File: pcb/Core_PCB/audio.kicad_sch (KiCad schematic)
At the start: 3 parts, among them J1 Screw_Terminal_01x02, U1 MAX98357A

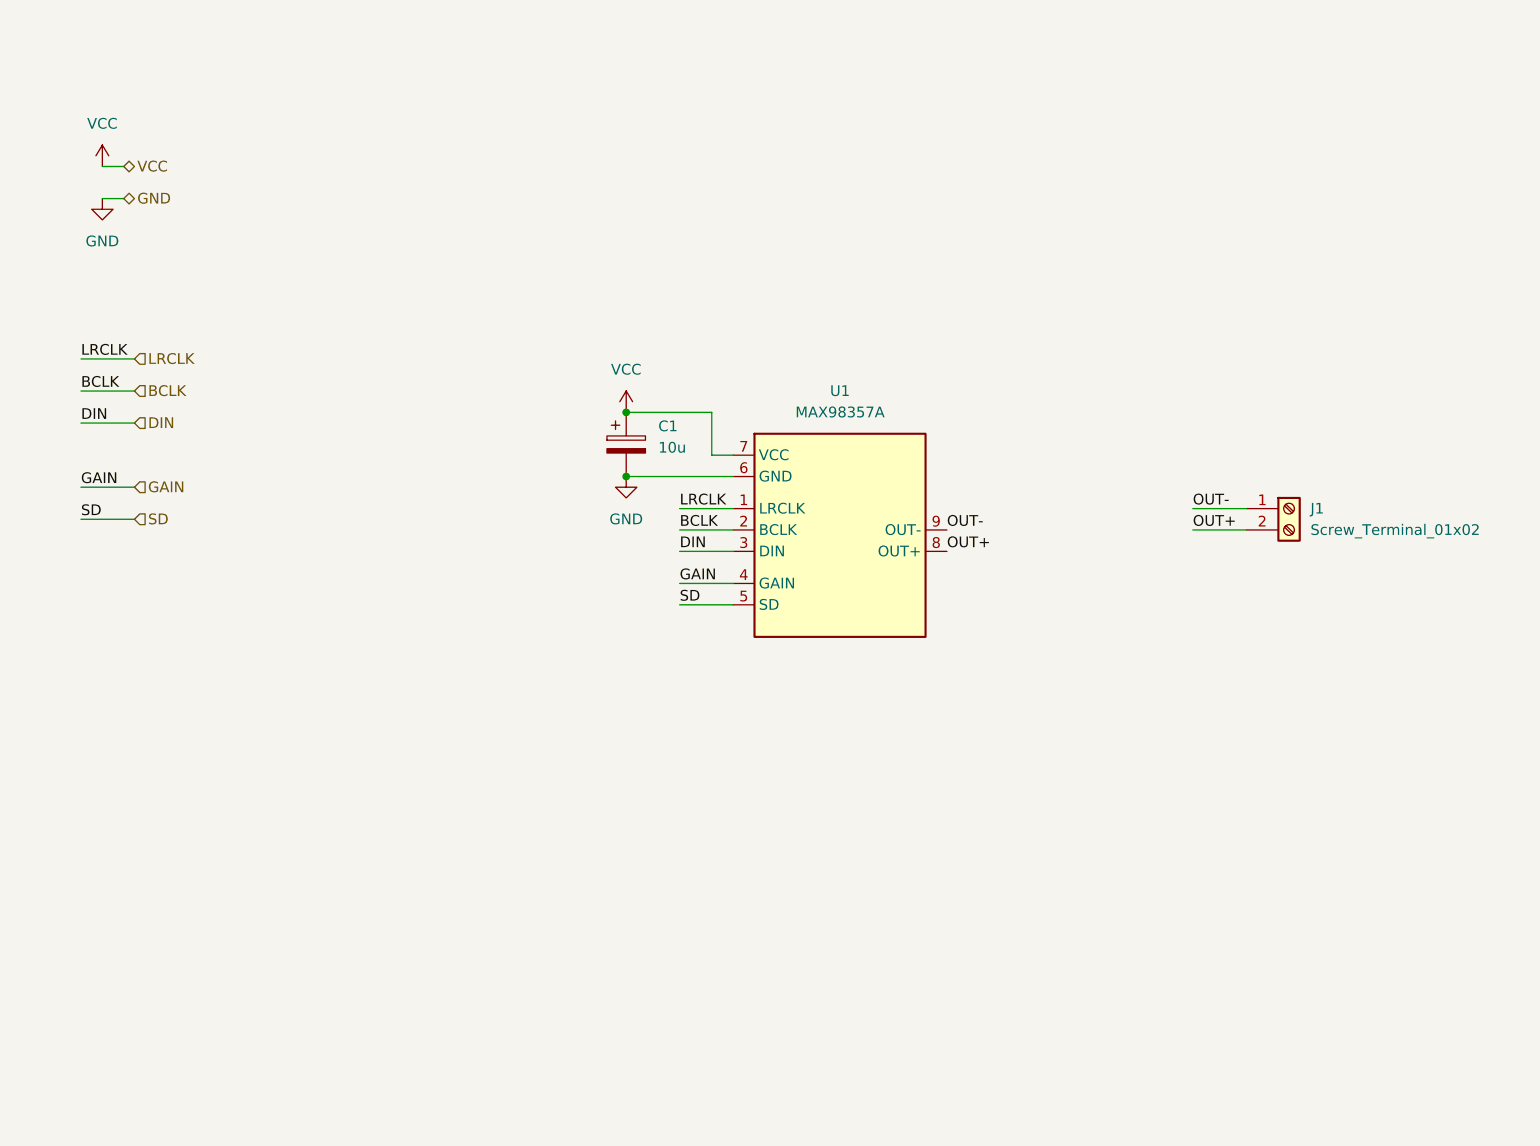
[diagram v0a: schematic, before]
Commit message: SCH: audio gain control via mux (HEF4051), buttons read via i2c io expander (MCP23017)
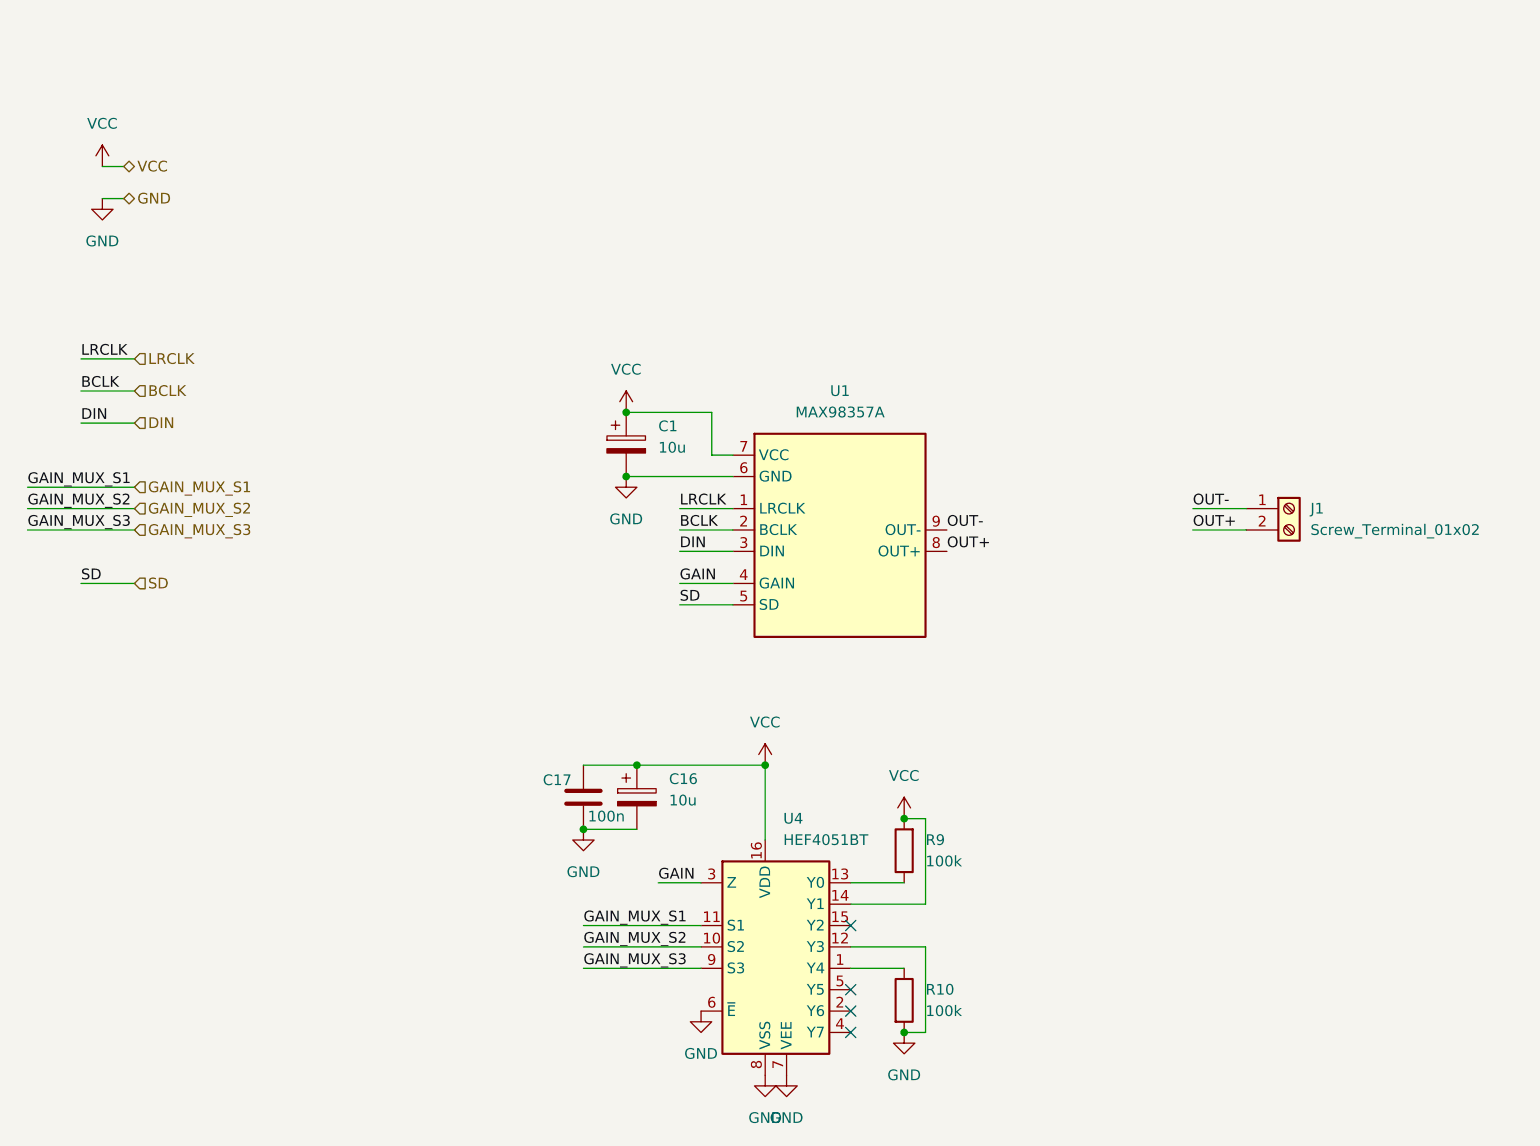
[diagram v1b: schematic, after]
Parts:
- added C16: 10u, symbol Device:C_Polarized
- added C17: 100n, symbol Device:C
- added R10, R9: 100k, symbol Device:R
- added U4: HEF4051BT, Package_SO:SOIC-16_3.9x9.9mm_P1.27mm, symbol Analog_Switch:HEF4051BT
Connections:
- net GAIN: now also U4.3 (Z)
- net GND: now also C16.2, C17.2, R10.2, U4.12 (Y3), U4.6 (~{E}), U4.7 (VEE), U4.8 (VSS)
- net VCC: now also C16.1, C17.1, R9.2, U4.14 (Y1), U4.16 (VDD)
- new net: R10.1, U4.1 (Y4)
- new net: R9.1, U4.13 (Y0)
- new net GAIN_MUX_S1: U4.11 (S1)
- new net GAIN_MUX_S2: U4.10 (S2)
- new net GAIN_MUX_S3: U4.9 (S3)
- no-connect marks 0 -> 4

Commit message: SCH: annotated sheets, reannotated all components
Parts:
- J6: renamed from J1; Name (none) -> SPEAKER
- renumbered C1 to C4, C17 to C5, C16 to C6, R9 to R1, R10 to R2, U4 to U2
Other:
- company: (none) -> brunolalb@gmail.com
- title: (none) -> Alarm Clock Resto Mod - Core PCB
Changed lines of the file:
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@@
 	(generator_version "10.0")
 	(paper "A4")
+	(title_block
+		(title "Alarm Clock Resto Mod - Core PCB")
+		(date "2026-07-08")
+		(rev "1.0")
+		(company "brunolalb@gmail.com")
+		(comment 1 "Bruno Landau Albrecht")
+	)
 	(junction
 		(at 102.87 76.2)
@@
 		(in_pos_files yes)
 		(dnp no)
-		(property "Reference" "C17"
+		(property "Reference" "C5"
 			(at 92.964 112.268 0)
 			(show_name no)
@@
 			(project "Core_PCB"
 				(path "/79975d02-cfea-4cc3-8869-9743c86248b2/277cf276-8816-41e6-a7a7-65f79c8908df"
-					(reference "C17")
+					(reference "C5")
 					(unit 1)
 				)
@@
 		(dnp no)
 		(fields_autoplaced yes)
-		(property "Reference" "#PWR014"
+		(property "Reference" "#PWR024"
 			(at 40.64 49.53 0)
 			(hide yes)
@@
 			(project "Core_PCB"
 				(path "/79975d02-cfea-4cc3-8869-9743c86248b2/277cf276-8816-41e6-a7a7-65f79c8908df"
-					(reference "#PWR014")
+					(reference "#PWR024")
 					(unit 1)
 				)
@@
 		(dnp no)
 		(fields_autoplaced yes)
-		(property "Reference" "#PWR052"
+		(property "Reference" "#PWR031"
 			(at 135.89 148.59 0)
 			(hide yes)
@@
 			(project "Core_PCB"
 				(path "/79975d02-cfea-4cc3-8869-9743c86248b2/277cf276-8816-41e6-a7a7-65f79c8908df"
-					(reference "#PWR052")
+					(reference "#PWR031")
 					(unit 1)
 				)
@@
 		(dnp no)
 		(fields_autoplaced yes)
-		(property "Reference" "#PWR055"
+		(property "Reference" "#PWR029"
 			(at 97.79 124.46 0)
 			(hide yes)
@@
 			(project "Core_PCB"
 				(path "/79975d02-cfea-4cc3-8869-9743c86248b2/277cf276-8816-41e6-a7a7-65f79c8908df"
-					(reference "#PWR055")
+					(reference "#PWR029")
 					(unit 1)
 				)
@@
 		(dnp no)
 		(fields_autoplaced yes)
-		(property "Reference" "U4"
+		(property "Reference" "U2"
 			(at 121.5233 116.84 0)
 			(show_name no)
@@
 			(project "Core_PCB"
 				(path "/79975d02-cfea-4cc3-8869-9743c86248b2/277cf276-8816-41e6-a7a7-65f79c8908df"
-					(reference "U4")
+					(reference "U2")
 					(unit 1)
 				)
@@
 		(dnp no)
 		(fields_autoplaced yes)
-		(property "Reference" "C16"
+		(property "Reference" "C6"
 			(at 107.95 112.1409 0)
 			(show_name no)
@@
 			(project "Core_PCB"
 				(path "/79975d02-cfea-4cc3-8869-9743c86248b2/277cf276-8816-41e6-a7a7-65f79c8908df"
-					(reference "C16")
+					(reference "C6")
 					(unit 1)
 				)
@@
 		(dnp no)
 		(fields_autoplaced yes)
-		(property "Reference" "R9"
+		(property "Reference" "R1"
 			(at 138.43 119.3799 0)
 			(show_name no)
@@
 			(project "Core_PCB"
 				(path "/79975d02-cfea-4cc3-8869-9743c86248b2/277cf276-8816-41e6-a7a7-65f79c8908df"
-					(reference "R9")
+					(reference "R1")
 					(unit 1)
 				)
@@
 		(dnp no)
 		(fields_autoplaced yes)
-		(property "Reference" "#PWR013"
+		(property "Reference" "#PWR023"
 			(at 40.64 43.18 0)
 			(hide yes)
@@
 			(project "Core_PCB"
 				(path "/79975d02-cfea-4cc3-8869-9743c86248b2/277cf276-8816-41e6-a7a7-65f79c8908df"
-					(reference "#PWR013")
+					(reference "#PWR023")
 					(unit 1)
 				)
@@
 		(dnp no)
 		(fields_autoplaced yes)
-		(property "Reference" "#PWR051"
+		(property "Reference" "#PWR033"
 			(at 121.92 153.67 0)
 			(hide yes)
@@
 			(project "Core_PCB"
 				(path "/79975d02-cfea-4cc3-8869-9743c86248b2/277cf276-8816-41e6-a7a7-65f79c8908df"
-					(reference "#PWR051")
+					(reference "#PWR033")
 					(unit 1)
 				)
@@
 		(dnp no)
 		(fields_autoplaced yes)
-		(property "Reference" "#PWR046"
+		(property "Reference" "#PWR027"
 			(at 119.38 114.3 0)
 			(hide yes)
@@
 			(project "Core_PCB"
 				(path "/79975d02-cfea-4cc3-8869-9743c86248b2/277cf276-8816-41e6-a7a7-65f79c8908df"
-					(reference "#PWR046")
+					(reference "#PWR027")
 					(unit 1)
 				)
@@
 		(in_pos_files yes)
 		(dnp no)
-		(fields_autoplaced yes)
-		(property "Reference" "J1"
+		(property "Reference" "J6"
 			(at 184.15 80.0099 0)
 			(show_name no)
@@
 			(at 181.61 80.01 0)
 			(hide yes)
+			(show_name no)
+			(do_not_autoplace no)
+			(effects
+				(font
+					(size 1.27 1.27)
+				)
+			)
+		)
+		(property "Name" "SPEAKER"
+			(at 181.864 86.106 0)
 			(show_name no)
 			(do_not_autoplace no)
@@
 			(project "Core_PCB"
 				(path "/79975d02-cfea-4cc3-8869-9743c86248b2/277cf276-8816-41e6-a7a7-65f79c8908df"
-					(reference "J1")
+					(reference "J6")
 					(unit 1)
 				)
@@
 		(dnp no)
 		(fields_autoplaced yes)
-		(property "Reference" "C1"
+		(property "Reference" "C4"
 			(at 106.68 70.2309 0)
 			(show_name no)
@@
 			(project "Core_PCB"
 				(path "/79975d02-cfea-4cc3-8869-9743c86248b2/277cf276-8816-41e6-a7a7-65f79c8908df"
-					(reference "C1")
+					(reference "C4")
 					(unit 1)
 				)
@@
 		(dnp no)
 		(fields_autoplaced yes)
-		(property "Reference" "#PWR054"
+		(property "Reference" "#PWR030"
 			(at 111.76 146.05 0)
 			(hide yes)
@@
 			(project "Core_PCB"
 				(path "/79975d02-cfea-4cc3-8869-9743c86248b2/277cf276-8816-41e6-a7a7-65f79c8908df"
-					(reference "#PWR054")
+					(reference "#PWR030")
 					(unit 1)
 				)
@@
 		(dnp no)
 		(fields_autoplaced yes)
-		(property "Reference" "#PWR012"
+		(property "Reference" "#PWR026"
 			(at 102.87 82.55 0)
 			(hide yes)
@@
 			(project "Core_PCB"
 				(path "/79975d02-cfea-4cc3-8869-9743c86248b2/277cf276-8816-41e6-a7a7-65f79c8908df"
-					(reference "#PWR012")
+					(reference "#PWR026")
 					(unit 1)
 				)
@@
 		(dnp no)
 		(fields_autoplaced yes)
-		(property "Reference" "#PWR053"
+		(property "Reference" "#PWR028"
 			(at 135.89 120.65 0)
 			(hide yes)
@@
 			(project "Core_PCB"
 				(path "/79975d02-cfea-4cc3-8869-9743c86248b2/277cf276-8816-41e6-a7a7-65f79c8908df"
-					(reference "#PWR053")
+					(reference "#PWR028")
 					(unit 1)
 				)
@@
 		(dnp no)
 		(fields_autoplaced yes)
-		(property "Reference" "#PWR050"
+		(property "Reference" "#PWR032"
 			(at 119.38 153.67 0)
 			(hide yes)
@@
 			(project "Core_PCB"
 				(path "/79975d02-cfea-4cc3-8869-9743c86248b2/277cf276-8816-41e6-a7a7-65f79c8908df"
-					(reference "#PWR050")
+					(reference "#PWR032")
 					(unit 1)
 				)
@@
 		(dnp no)
 		(fields_autoplaced yes)
-		(property "Reference" "R10"
+		(property "Reference" "R2"
 			(at 138.43 137.1599 0)
 			(show_name no)
@@
 			(project "Core_PCB"
 				(path "/79975d02-cfea-4cc3-8869-9743c86248b2/277cf276-8816-41e6-a7a7-65f79c8908df"
-					(reference "R10")
+					(reference "R2")
 					(unit 1)
 				)
@@
 		(dnp no)
 		(fields_autoplaced yes)
-		(property "Reference" "#PWR011"
+		(property "Reference" "#PWR025"
 			(at 102.87 72.39 0)
 			(hide yes)
@@
 			(project "Core_PCB"
 				(path "/79975d02-cfea-4cc3-8869-9743c86248b2/277cf276-8816-41e6-a7a7-65f79c8908df"
-					(reference "#PWR011")
+					(reference "#PWR025")
 					(unit 1)
 				)

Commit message: SCH: assigned footprints to what had missing, replaced some polarized caps with non polarized, added connector for capacitance sensor, ran electric test and fixed minor issues
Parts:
- C4, C6: footprint (none) -> Capacitor_SMD:C_0805_2012Metric_Pad1.18x1.45mm_HandSolder; symbol Device:C_Polarized -> Device:C
- C5: footprint (none) -> Capacitor_SMD:C_0603_1608Metric_Pad1.08x0.95mm_HandSolder
- R1, R2: footprint (none) -> Resistor_SMD:R_0603_1608Metric_Pad0.98x0.95mm_HandSolder
- U1: footprint (none) -> RadioWecker:MAX98357A_Adafruit
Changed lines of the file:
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@@
 			)
 		)
-		(property "Footprint" ""
+		(property "Footprint" "Capacitor_SMD:C_0603_1608Metric_Pad1.08x0.95mm_HandSolder"
 			(at 98.7552 118.11 0)
 			(hide yes)
@@
 			)
 		)
-		(property "Footprint" ""
+		(property "Footprint" "RadioWecker:MAX98357A_Adafruit"
 			(at 118.11 95.25 0)
 			(hide yes)
@@
 	)
 	(symbol
-		(lib_id "Device:C_Polarized")
+		(lib_id "Device:C")
 		(at 104.14 114.3 0)
 		(unit 1)
@@
 		(fields_autoplaced yes)
 		(property "Reference" "C6"
-			(at 107.95 112.1409 0)
+			(at 107.95 113.0299 0)
 			(show_name no)
 			(do_not_autoplace no)
@@
 		)
 		(property "Value" "10u"
-			(at 107.95 114.6809 0)
+			(at 107.95 115.5699 0)
 			(show_name no)
 			(do_not_autoplace no)
@@
 			)
 		)
-		(property "Footprint" ""
+		(property "Footprint" "Capacitor_SMD:C_0805_2012Metric_Pad1.18x1.45mm_HandSolder"
 			(at 105.1052 118.11 0)
 			(hide yes)
@@
 			)
 		)
-		(property "Description" "Polarized capacitor"
+		(property "Description" "Unpolarized capacitor"
 			(at 104.14 114.3 0)
 			(hide yes)
@@
 			)
 		)
-		(property "Footprint" ""
+		(property "Footprint" "Resistor_SMD:R_0603_1608Metric_Pad0.98x0.95mm_HandSolder"
 			(at 137.668 120.65 90)
 			(hide yes)
@@
 	)
 	(symbol
-		(lib_id "Device:C_Polarized")
+		(lib_id "Device:C")
 		(at 102.87 72.39 0)
 		(unit 1)
@@
 		(fields_autoplaced yes)
 		(property "Reference" "C4"
-			(at 106.68 70.2309 0)
+			(at 106.68 71.1199 0)
 			(show_name no)
 			(do_not_autoplace no)
@@
 		)
 		(property "Value" "10u"
-			(at 106.68 72.7709 0)
+			(at 106.68 73.6599 0)
 			(show_name no)
 			(do_not_autoplace no)
@@
 			)
 		)
-		(property "Footprint" ""
+		(property "Footprint" "Capacitor_SMD:C_0805_2012Metric_Pad1.18x1.45mm_HandSolder"
 			(at 103.8352 76.2 0)
 			(hide yes)
@@
 			)
 		)
-		(property "Description" "Polarized capacitor"
+		(property "Description" "Unpolarized capacitor"
 			(at 102.87 72.39 0)
 			(hide yes)
@@
 			)
 		)
-		(property "Footprint" ""
+		(property "Footprint" "Resistor_SMD:R_0603_1608Metric_Pad0.98x0.95mm_HandSolder"
 			(at 134.112 138.43 90)
 			(hide yes)

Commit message: SCH - audio: screw terminal was facing the wrong direction; buttons: volume pot had wrong footprint, added +5V input; processor: use alternative arduino symbol and custom footprint (with 3d model), added reset switch, adjusted rule for PWR lines
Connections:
- net OUT+: now also J6.1 (Pin_1); no longer J6.2 (Pin_2)
- net OUT-: now also J6.2 (Pin_2); no longer J6.1 (Pin_1)
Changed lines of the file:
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@@
+	)
+	(symbol
+		(lib_id "Connector:Screw_Terminal_01x02")
+		(at 181.61 82.55 0)
+		(mirror x)
+		(unit 1)
+		(body_style 1)
+		(exclude_from_sim no)
+		(in_bom yes)
+		(on_board yes)
+		(in_pos_files yes)
+		(dnp no)
+		(property "Reference" "J6"
+			(at 184.15 82.5501 0)
+			(show_name no)
+			(do_not_autoplace no)
+			(effects
+				(font
+					(size 1.27 1.27)
+				)
+				(justify left)
+			)
+		)
+		(property "Value" "Screw_Terminal_01x02"
+			(at 184.15 80.0101 0)
+			(show_name no)
+			(do_not_autoplace no)
+			(effects
+				(font
+					(size 1.27 1.27)
+				)
+				(justify left)
+			)
+		)
+		(property "Footprint" "TerminalBlock_Phoenix:TerminalBlock_Phoenix_PT-1,5-2-3.5-H_1x02_P3.50mm_Horizontal"
+			(at 181.61 82.55 0)
+			(hide yes)
+			(show_name no)
+			(do_not_autoplace no)
+			(effects
+				(font
+					(size 1.27 1.27)
+				)
+			)
+		)
+		(property "Datasheet" ""
+			(at 181.61 82.55 0)
+			(hide yes)
+			(show_name no)
+			(do_not_autoplace no)
+			(effects
+				(font
+					(size 1.27 1.27)
+				)
+			)
+		)
+		(property "Description" "Generic screw terminal, single row, 01x02, script generated (kicad-library-utils/schlib/autogen/connector/)"
+			(at 181.61 82.55 0)
+			(hide yes)
+			(show_name no)
+			(do_not_autoplace no)
+			(effects
+				(font
+					(size 1.27 1.27)
+				)
+			)
+		)
+		(property "Name" "SPEAKER"
+			(at 181.864 76.454 0)
+			(show_name no)
+			(do_not_autoplace no)
+			(effects
+				(font
+					(size 1.27 1.27)
+				)
+			)
+		)
+		(pin "2"
+		)
+		(pin "1"
+		)
+		(instances
+			(project "Core_PCB"
+				(path "/79975d02-cfea-4cc3-8869-9743c86248b2/277cf276-8816-41e6-a7a7-65f79c8908df"
+					(reference "J6")
+					(unit 1)
+				)
+			)
+		)
 	)
 	(symbol
@@
 					(unit 1)
 				)
-			)
-		)
-	)
-	(symbol
-		(lib_id "Connector:Screw_Terminal_01x02")
-		(at 181.61 80.01 0)
-		(unit 1)
-		(body_style 1)
-		(exclude_from_sim no)
-		(in_bom yes)
-		(on_board yes)
-		(in_pos_files yes)
-		(dnp no)
-		(property "Reference" "J6"
-			(at 184.15 80.0099 0)
-			(show_name no)
-			(do_not_autoplace no)
-			(effects
-				(font
-					(size 1.27 1.27)
-				)
-				(justify left)
-			)
-		)
-		(property "Value" "Screw_Terminal_01x02"
-			(at 184.15 82.5499 0)
-			(show_name no)
-			(do_not_autoplace no)
-			(effects
-				(font
-					(size 1.27 1.27)
-				)
-				(justify left)
-			)
-		)
-		(property "Footprint" "TerminalBlock_Phoenix:TerminalBlock_Phoenix_PT-1,5-2-3.5-H_1x02_P3.50mm_Horizontal"
-			(at 181.61 80.01 0)
-			(hide yes)
-			(show_name no)
-			(do_not_autoplace no)
-			(effects
-				(font
-					(size 1.27 1.27)
-				)
-			)
-		)
-		(property "Datasheet" ""
-			(at 181.61 80.01 0)
-			(hide yes)
-			(show_name no)
-			(do_not_autoplace no)
-			(effects
-				(font
-					(size 1.27 1.27)
-				)
-			)
-		)
-		(property "Description" "Generic screw terminal, single row, 01x02, script generated (kicad-library-utils/schlib/autogen/connector/)"
-			(at 181.61 80.01 0)
-			(hide yes)
-			(show_name no)
-			(do_not_autoplace no)
-			(effects
-				(font
-					(size 1.27 1.27)
-				)
-			)
-		)
-		(property "Name" "SPEAKER"
-			(at 181.864 86.106 0)
-			(show_name no)
-			(do_not_autoplace no)
-			(effects
-				(font
-					(size 1.27 1.27)
-				)
-			)
-		)
-		(pin "2"
-		)
-		(pin "1"
-		)
-		(instances
-			(project "Core_PCB"
-				(path "/79975d02-cfea-4cc3-8869-9743c86248b2/277cf276-8816-41e6-a7a7-65f79c8908df"
-					(reference "J6")
-					(unit 1)
-				)

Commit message: use a potentiometer connector (picoblade) and moved it to the audio sch; touch interface (capacitance measureer) got a 2 row connector with GND on one line; added mounting screws and logo to the main sch (and lib)
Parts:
- added C8: 100n, Capacitor_SMD:C_0603_1608Metric_Pad1.08x0.95mm_HandSolder, symbol Device:C
- added J11: Conn_01x03_MountingPin, Connector_Molex:Molex_PicoBlade_53261-0371_1x03-1MP_P1.25mm_Horizontal, symbol Connector_Generic_MountingPin:Conn_01x03_MountingPin
- added R3: 1k, Resistor_SMD:R_0603_1608Metric_Pad0.98x0.95mm_HandSolder, symbol Device:R
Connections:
- net GND: now also C8.2, J11.3 (Pin_3), J11.MP (MountPin)
- new net: J11.2 (Pin_2), R3.1
- new net +3V3: J11.1 (Pin_1)
- new net VOLUME_POT: C8.1, R3.2

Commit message: SCH: audio - forgot the +3V3 hierarchical label, renamed VCC to +5V, made screw terminal not populated (use the one on the i2s module) SCH general: bumped date
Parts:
- J6: now not fitted
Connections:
- net VCC renamed +5V
